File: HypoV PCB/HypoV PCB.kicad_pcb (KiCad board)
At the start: 2 copper layers, 61.5 x 43 mm, 12 parts, among them J1 Conn_Header_JST_PH_1x02_P2mm_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

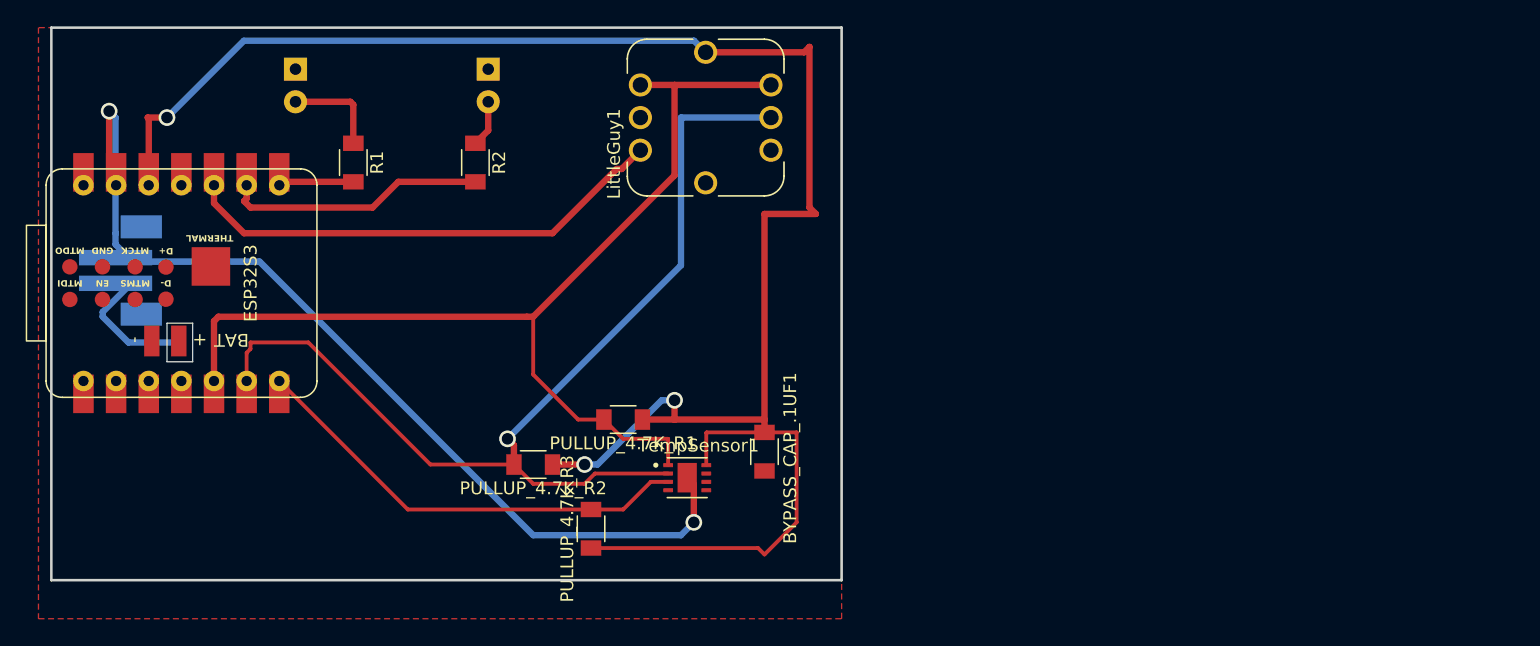
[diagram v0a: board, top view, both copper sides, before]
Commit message: added the breakout board
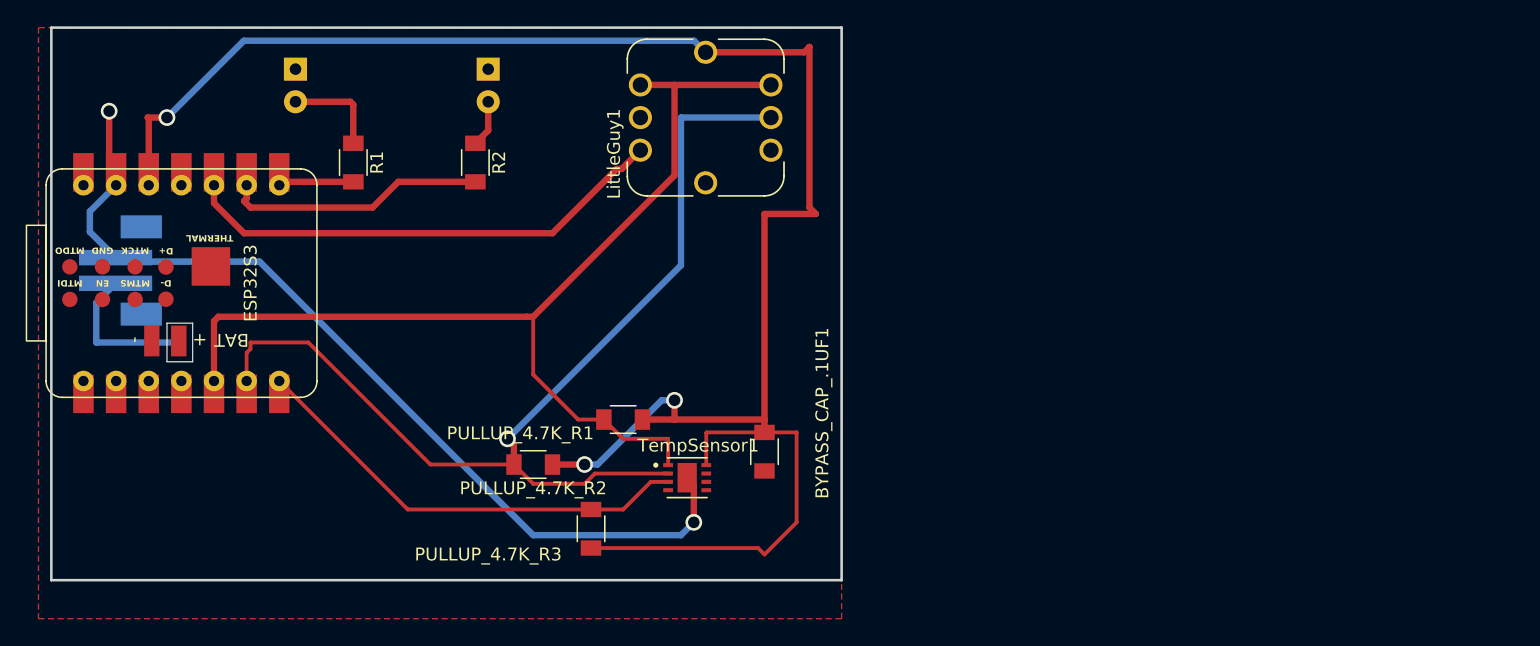
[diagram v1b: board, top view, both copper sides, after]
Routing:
- net GND: track 73.9 -> 69.0 mm
- net Net-(ESP32S3-BAT_VIN): track 10.4 -> 11.9 mm
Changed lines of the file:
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@@
 			(outputformat 1)
 			(mirror no)
-			(drillshape 1)
+			(drillshape 0)
 			(scaleselection 1)
 			(outputdirectory "")
@@
 		(tags "resistor 1206")
 		(property "Reference" "PULLUP_4.7K_R3"
-			(at 0 -1.85 90)
+			(at -2 -8 0)
 			(layer "F.SilkS")
 			(effects
@@
 		)
 		(property "Value" "MAX30205MTA+T"
-			(at 9.755 2.362 0)
+			(at 5.015 5.975 0)
 			(layer "F.Fab")
 			(effects
@@
 		(tags "resistor 1206")
 		(property "Reference" "PULLUP_4.7K_R1"
-			(at 0 -1.85 0)
+			(at 8 -1.07 0)
 			(layer "F.SilkS")
 			(effects
@@
 		)
 		(fp_text user "${REFERENCE}"
-			(at 0 0 0)
+			(at 0 1.07 0)
 			(layer "F.Fab")
 			(effects
@@
 		)
 		(fp_text user "${REFERENCE}"
-			(at 0.0025 2.931 90)
+			(at 0.0025 10.551 90)
 			(unlocked yes)
 			(layer "F.Fab")
@@
 		(tags "capacitor 1206")
 		(property "Reference" "BYPASS_CAP_.1UF1"
-			(at 0.5 -2 90)
+			(at -3 -4.5 90)
 			(layer "F.SilkS")
 			(effects
@@
 		)
 		(fp_text user "${REFERENCE}"
-			(at 0 0 90)
+			(at 0.475 -1.07 90)
 			(layer "F.Fab")
 			(effects
@@
 		)
 		(property "Value" "Conn_Header_JST_PH_1x02_P2mm_Vertical_SMD"
-			(at 0 0.5 0)
+			(at -15.671 -0.9825 0)
 			(layer "B.Fab")
 			(effects
@@
 	)
 	(segment
-		(start 76 86.875)
-		(end 77.125 88)
+		(start 74 85.9)
+		(end 76 87.9)
 		(width 0.5)
 		(layer "B.Cu")
@@
 	)
 	(segment
-		(start 76 77)
-		(end 76 86)
+		(start 74 84.305)
+		(end 74 85.9)
 		(width 0.5)
 		(layer "B.Cu")
@@
 	)
 	(segment
-		(start 76 86)
-		(end 76 86.875)
+		(start 76.04 82.265)
+		(end 74 84.305)
 		(width 0.5)
 		(layer "B.Cu")
@@
 	)
 	(segment
-		(start 75.5 76.5)
-		(end 76 77)
-		(width 0.5)
-		(layer "B.Cu")
-		(net 1)
-	)
-	(segment
 		(start 100.5 104)
 		(end 107 104)
@@
 	)
 	(segment
-		(start 75 92.5)
-		(end 75 92.125)
+		(start 76 89.9)
+		(end 74.5 91.4)
 		(width 0.5)
 		(layer "B.Cu")
@@
 	)
 	(segment
-		(start 77 94.5)
-		(end 75 92.5)
-		(width 0.5)
-		(layer "B.Cu")
-		(net 14)
-	)
-	(segment
-		(start 75 92.125)
-		(end 77.125 90)
+		(start 74.5 94.5)
+		(end 81 94.5)
 		(width 0.5)
 		(layer "B.Cu")
@@
 	)
 	(segment
-		(start 81 94.5)
-		(end 77 94.5)
+		(start 74.5 91.4)
+		(end 74.5 94.5)
 		(width 0.5)
 		(layer "B.Cu")
@@
 		(hatch edge 0.5)
 		(connect_pads
-			(clearance 0.5)
+			(clearance 0.7)
 		)
-		(min_thickness 0.25)
+		(min_thickness 0.5)
 		(filled_areas_thickness no)
 		(fill yes

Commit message: added final pcb
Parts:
- removed BYPASS_CAP_.1UF1: C_1206, PCM_fab:C_1206
- removed PULLUP_4.7K_R1, PULLUP_4.7K_R2, PULLUP_4.7K_R3: R_1206, PCM_fab:R_1206
- removed TempSensor1: MAX30205MTA+T, MAX30205MTA_T:SON65P300X300X80-9N
- added .1UF_C: C, Capacitor_SMD:C_0805_2012Metric_Pad1.18x1.45mm_HandSolder, F.Cu at (162.5, 94.5)
- added 4.7K_R: R, Resistor_SMD:R_0805_2012Metric_Pad1.20x1.40mm_HandSolder, F.Cu at (144.5, 96.5)
- added 4.7K_R2: R, Resistor_SMD:R_0805_2012Metric_Pad1.20x1.40mm_HandSolder, F.Cu at (154.0, 91.0)
- added 4.7K_R3: R, Resistor_SMD:R_0805_2012Metric_Pad1.20x1.40mm_HandSolder, F.Cu at (145.0, 92.0)
- added J1: Conn_01x05_Pin, Connector_PinSocket_2.54mm:PinSocket_1x05_P2.54mm_Vertical, F.Cu at (172.9, 90.6)
- added J2: Conn_01x05_Pin, Connector_PinHeader_2.54mm:PinHeader_1x05_P2.54mm_Vertical, B.Cu at (124.5, 95.8)
- added J3: Conn_01x05_Pin, Connector_PinSocket_2.54mm:PinSocket_1x05_P2.54mm_Vertical, F.Cu at (149.0, 90.3)
- added U1: MAX30205, footprints:21-0137_T833&plus_2_MXM-M, F.Cu at (158.0, 96.0)
- added U2: MAX30205, footprints:21-0137_T833&plus_2_MXM-M, F.Cu at (178.5, 95.9)
- BLUE_LED1, RED_LED1: moved to F.Cu
- LittleGuy1: moved to B.Cu
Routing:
- net +3.3V: track 150.4 -> 87.8 mm, vias 3 -> 1
- net +3V3: track 0.00 -> 31.8 mm
- net GND2: track 0.00 -> 16.7 mm
- net Net-(J3-Pin_4): track 0.00 -> 14.9 mm
- net Net-(J3-Pin_3): track 0.00 -> 12.5 mm
- net GND: track 69.0 -> 80.1 mm, vias 2 -> 1
- net +3V32: track 0.00 -> 10.9 mm
- net Net-(J3-Pin_2): track 0.00 -> 9.36 mm
- net /OS: track 35.3 -> 41.6 mm
- net Net-(J1-Pin_2): track 0.00 -> 5.48 mm
- net Net-(J1-Pin_4): track 0.00 -> 5.31 mm
- net Net-(J1-Pin_3): track 0.00 -> 4.10 mm
- net /SDA: track 81.5 -> 84.4 mm
- net /SCL: vias 1 -> 0
- added copper zone on F.Cu, net (none)
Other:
- board size 61.5 x 43 mm -> 113 x 43 mm
- board text added: "3.3"
- board text added: "3.3V"
- board text added: "OS"
- board text added: "SCL"
- board text added: "SDA"
